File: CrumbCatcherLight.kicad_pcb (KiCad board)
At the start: 2 copper layers, 79.4 x 91.8 mm, 78 parts, among them J1 USB_C_Receptacle_USB2.0, J2 Conn_ARM_SWD_TagConnect_TC203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, Q1 2N7002VC-7, SW10 SW_SPST, SW11 SW_SPST, SW12 SW_SPST, SW13 SW_SPST, SW14 SW_SPST, SW15 SW_SPST, SW16 SW_SPST, SW17 SW_SPST, SW2 SW_SPST, SW3 SW_SPST, SW4 SW_SPST, SW5 SW_SPST, SW6 SW_SPST, SW7 SW_SPST, SW8 SW_SPST, SW9 SW_SPST, U1 ECMF02-2AMX6, U2 XC6206PxxxMR-Regulator_Linear, U3 GD25LQ128DYIGR, U4 RP2040, Y1 12MHz

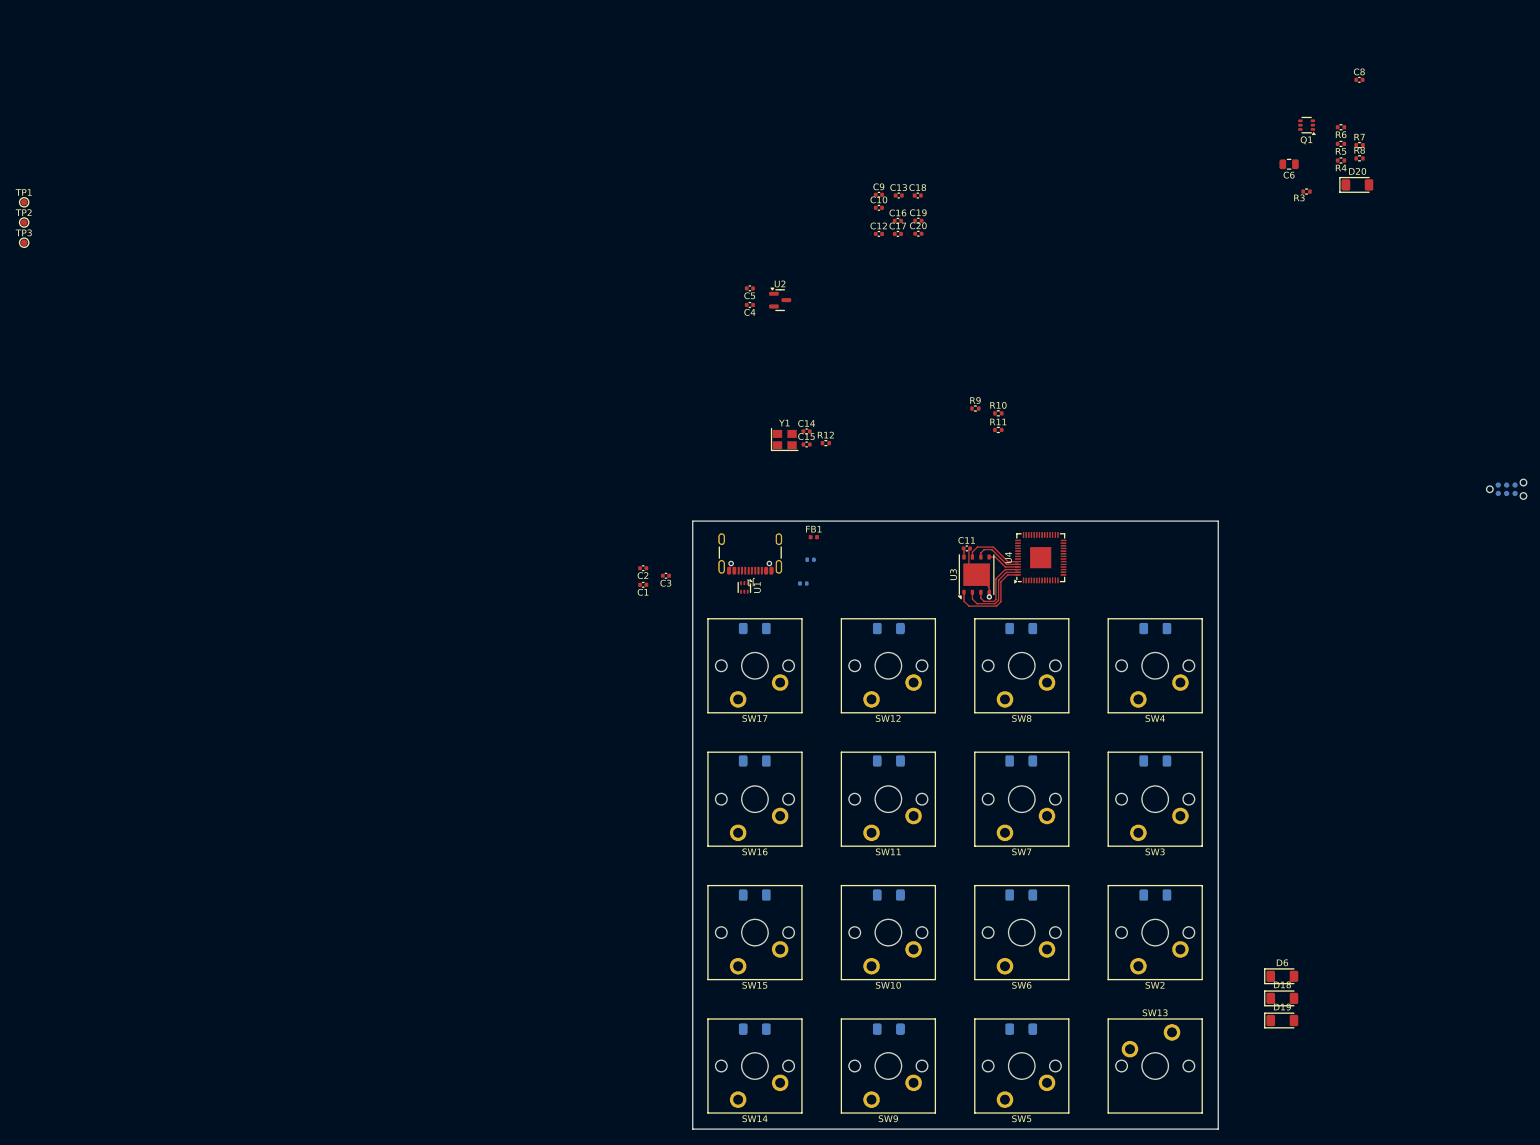
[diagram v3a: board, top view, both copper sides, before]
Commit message: Select last few components, add and cleanup footprints
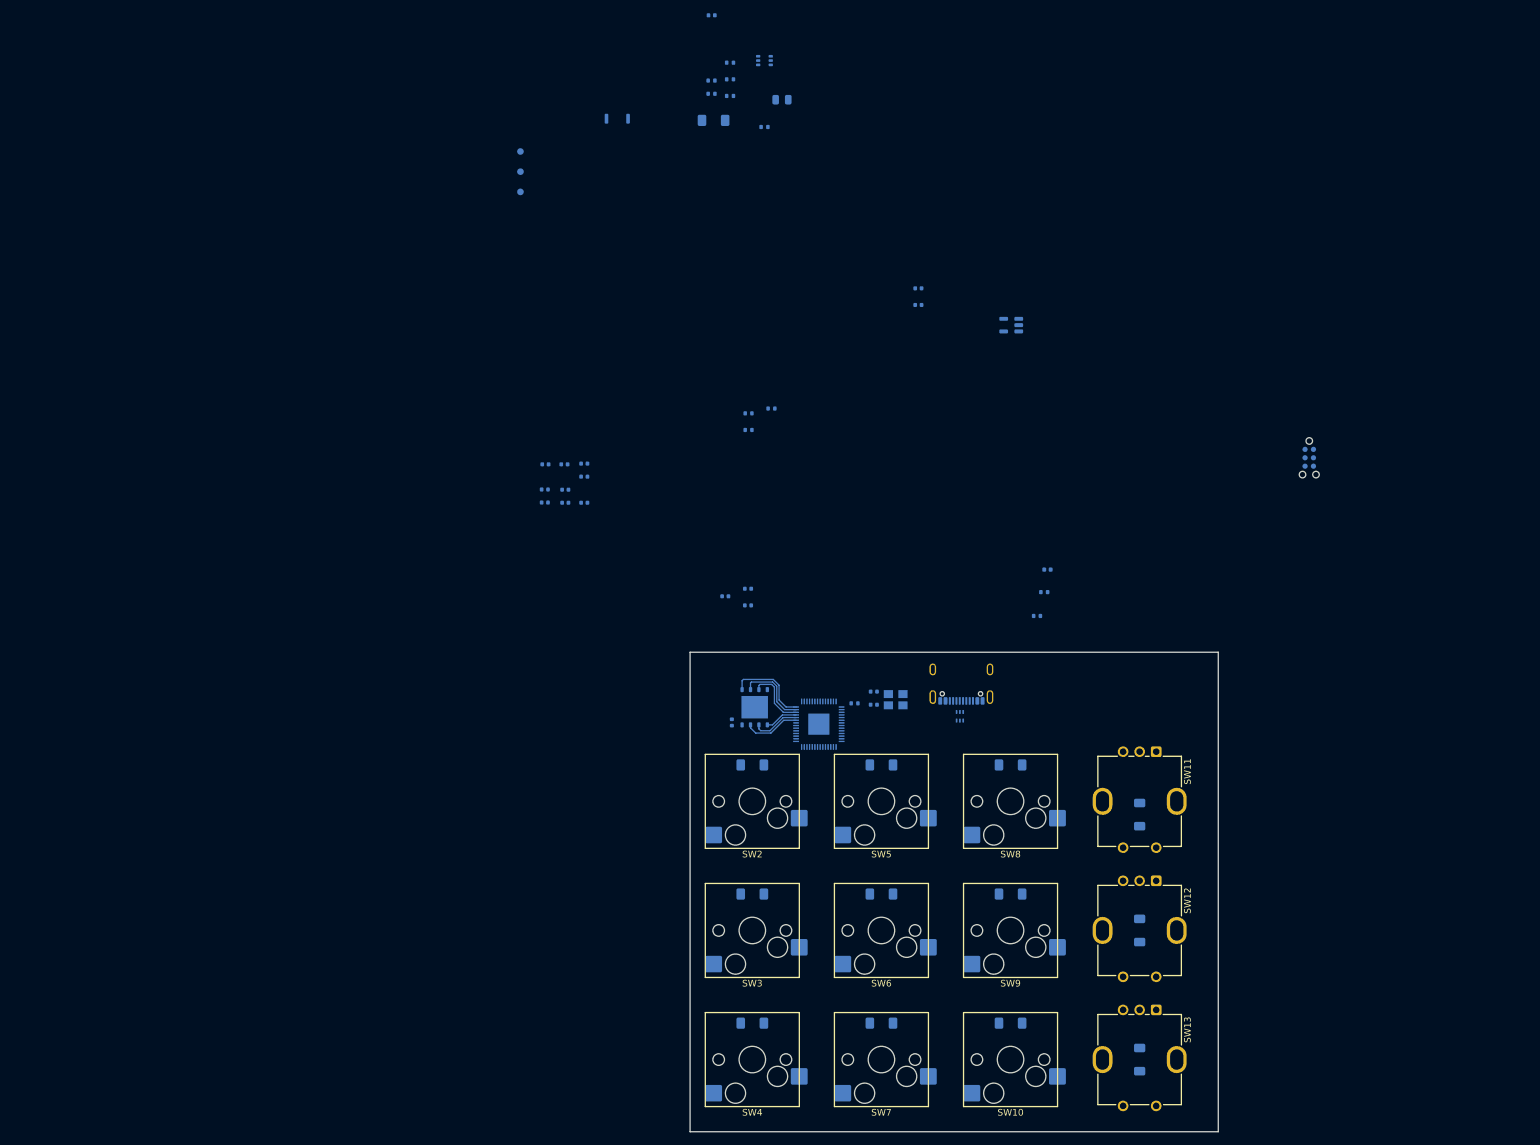
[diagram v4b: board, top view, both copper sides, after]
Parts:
- removed the D13 at (131.6, 105.7)
- removed D14, D15, D16, D17: LL4148, Diode_SMD:D_MiniMELF
- removed the D5 at (151.6, 125.9)
- removed the D9 at (151.6, 85.4)
- removed SW14, SW15, SW16, SW17: SW_SPST, PCM_Switch_Keyboard_Cherry_MX:SW_Cherry_MX_PCB_1.00u
- removed the SW5 at (151.7, 131.5)
- removed the SW8 at (151.7, 71.0)
- removed U2: XC6206PxxxMR-Regulator_Linear, Package_TO_SOT_SMD:SOT-23
- added D12: LL4148, Diode_SMD:D_MiniMELF, B.Cu at (169.5, 111.0)
- added SW1: TL3780AF240QG, Mad_Footprints:SW_TL3780AF240QG, B.Cu at (90.6, -11.6)
- added SW11: PEC11R, Mad_Footprints:RotaryEncoder_Bourns_Vertical_PEC12R-3x17F-Sxxxx, F.Cu at (169.5, 91.5)
- added SW12: PEC11R, Mad_Footprints:RotaryEncoder_Bourns_Vertical_PEC12R-3x17F-Sxxxx, F.Cu at (169.5, 111.0)
- added U5: XC6210B332MR, Package_TO_SOT_SMD:SOT-23-5, B.Cu at (150.1, 19.6)
- C1, C2, C3, C4, C5, C6, D6, FB1, J1, Q1, R10, R11, R12, R3, R4, R5, R6, R7, R8, R9, TP1, TP2, TP3, U1, U3, U4, Y1: moved to B.Cu
- C10: renamed from C11; moved to B.Cu
- C11: renamed from C12; moved to B.Cu
- C12: renamed from C13; moved to B.Cu
- C13: renamed from C14; moved to B.Cu
- C14: renamed from C15; moved to B.Cu
- C15: renamed from C16; moved to B.Cu
- C16: renamed from C17; moved to B.Cu
- C17: renamed from C18; moved to B.Cu
- C18: renamed from C19; moved to B.Cu
- C19: renamed from C20; moved to B.Cu
- C7: renamed from C8; moved to B.Cu
- C8: renamed from C9; moved to B.Cu
- C9: renamed from C10; moved to B.Cu
- D1: renamed from D20; moved to B.Cu
- D11: renamed from D18; moved to B.Cu
- D13: renamed from D19; moved to B.Cu
- SW10: renamed from SW2; footprint PCM_Switch_Keyboard_Cherry_MX:SW_Cherry_MX_PCB_1.00u -> Mad_Footprints:SW_Hotswap_Kailh_MX_1.00u
- SW13: value SW_SPST -> PEC11R; footprint PCM_Switch_Keyboard_Cherry_MX:SW_Cherry_MX_PCB_1.00u -> Mad_Footprints:RotaryEncoder_Bourns_Vertical_PEC12R-3x17F-Sxxxx
- SW2: renamed from SW12; footprint PCM_Switch_Keyboard_Cherry_MX:SW_Cherry_MX_PCB_1.00u -> Mad_Footprints:SW_Hotswap_Kailh_MX_1.00u
- SW3: renamed from SW11; footprint PCM_Switch_Keyboard_Cherry_MX:SW_Cherry_MX_PCB_1.00u -> Mad_Footprints:SW_Hotswap_Kailh_MX_1.00u
- SW4: renamed from SW10; footprint PCM_Switch_Keyboard_Cherry_MX:SW_Cherry_MX_PCB_1.00u -> Mad_Footprints:SW_Hotswap_Kailh_MX_1.00u
- SW5: renamed from SW9; footprint PCM_Switch_Keyboard_Cherry_MX:SW_Cherry_MX_PCB_1.00u -> Mad_Footprints:SW_Hotswap_Kailh_MX_1.00u
- SW6: renamed from SW7; footprint PCM_Switch_Keyboard_Cherry_MX:SW_Cherry_MX_PCB_1.00u -> Mad_Footprints:SW_Hotswap_Kailh_MX_1.00u
- SW7: renamed from SW6; footprint PCM_Switch_Keyboard_Cherry_MX:SW_Cherry_MX_PCB_1.00u -> Mad_Footprints:SW_Hotswap_Kailh_MX_1.00u
- SW8: renamed from SW4; footprint PCM_Switch_Keyboard_Cherry_MX:SW_Cherry_MX_PCB_1.00u -> Mad_Footprints:SW_Hotswap_Kailh_MX_1.00u
- SW9: renamed from SW3; footprint PCM_Switch_Keyboard_Cherry_MX:SW_Cherry_MX_PCB_1.00u -> Mad_Footprints:SW_Hotswap_Kailh_MX_1.00u
- moved R7 98.4 mm to (104.8, -17.4), turned to 180 degrees
- moved R8 98.4 mm to (104.8, -15.4), turned to 180 degrees
- moved C7 98.3 mm to (104.9, -27.2), turned to 180 degrees
- moved D1 97.7 mm to (105.2, -11.3), turned to 180 degrees
- moved R4 92.8 mm to (107.6, -15.0), turned to 0 degrees
- moved R5 92.8 mm to (107.6, -17.6), turned to 0 degrees
- moved R6 92.8 mm to (107.6, -20.1), turned to 0 degrees
- moved Q1 82.5 mm to (112.8, -20.4), turned to 0 degrees
- moved R3 82.4 mm to (112.8, -10.3), turned to 0 degrees
- moved C6 77.2 mm to (115.5, -14.5), turned to 0 degrees
- moved TP1 75.3 mm to (76.0, -6.65), turned to 180 degrees
- moved TP2 75.3 mm to (76.0, -3.60), turned to 180 degrees
- moved TP3 75.3 mm to (76.0, -0.55), turned to 180 degrees
- moved C18 69.5 mm to (79.7, 44.4), turned to 180 degrees
- moved C19 69.5 mm to (79.7, 46.4), turned to 180 degrees
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- renumbered D2 to D10, D12 to D2, D11 to D3, D10 to D4, D7 to D5, D8 to D7, D4 to D8, D3 to D9
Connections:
- D10 pad 1: Row1 -> Row2
- D11 pad 1: Row1 -> Row0
- D13 pad 1: Row3 -> Row2
- D13 pad 2: Net-(D19-A) -> Net-(D13-A)
- D2 pad 1: Row3 -> Row0
- D3 pad 1: Row2 -> Row1
- D4 pad 1: Row1 -> Row2
- D5 pad 1: Row2 -> Row0
- D7 pad 1: Row3 -> Row2
- D8 pad 1: Row3 -> Row0
- D9 pad 1: Row2 -> Row1
- SW10 pad 2: Col0 -> Col2
- SW2 pad 2: Col2 -> Col0
- SW3 pad 2: Col2 -> Col0
- SW4 pad 2: Col2 -> Col0
- SW8 pad 2: Col0 -> Col2
- SW9 pad 2: Col0 -> Col2
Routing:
- net GND: track 10.4 -> 3.33 mm, vias 1 -> 0
- net IOVDD: track 1.32 -> 0.00 mm
- net /RP2040/QSPI_SD2: track 10.5 -> 9.48 mm
- net /RP2040/QSPI_nCS: track 13.5 -> 12.6 mm
- net /RP2040/QSPI_SD1: track 11.9 -> 11.0 mm
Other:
- board size 79.4 x 91.8 mm -> 79.8 x 72.4 mm

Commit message: Update lib, finish off rotary encoder schematic, reselect diode for reset circuit
Update RP2040, rename bom only footprint, add mechanical footprint. Add PCB symbol
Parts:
- removed D1: LL4148, Diode_SMD:D_MiniMELF
- added D14: RB520S30, Diode_SMD:D_SOD-523, B.Cu at (111.3, -15.6)
- added R13: 2K2, Resistor_SMD:R_0402_1005Metric, B.Cu at (121.1, 53.7)
- added R14: 5K1, Resistor_SMD:R_0402_1005Metric, B.Cu at (121.1, 55.6)
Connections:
- net /RP2040/GPIO0 renamed /RP2040/0_TX0
- net /RP2040/GPIO1 renamed /RP2040/1_RX0
- net /RP2040/GPIO2 renamed /RP2040/2_SDA1
- net /RP2040/GPIO26 renamed /RP2040/A0
- net /RP2040/GPIO27 renamed /RP2040/A1
- net /RP2040/GPIO28 renamed /RP2040/A2
- net /RP2040/GPIO29 renamed /RP2040/A3
- net /RP2040/GPIO3 renamed /RP2040/3_SCL1
- net /RP2040/GPIO4 renamed /RP2040/4
- net /RP2040/GPIO5 renamed /RP2040/5
- net /RP2040/GPIO6 renamed /RP2040/6
- net /RP2040/GPIO7 renamed /RP2040/7
- net /RP2040/GPIO8 renamed /RP2040/8
- net /RP2040/GPIO9 renamed /RP2040/9
- net Col0 renamed /Switches/Col0
- net Col1 renamed /Switches/Col1
- net Col2 renamed /Switches/Col2
- net Col3 renamed /Switches/Col3
- net Row0 renamed /Switches/Row0
- net Row1 renamed /Switches/Row1
- net Row2 renamed /Switches/Row2
- SW11 pad A: unconnected-(SW11-PadA) -> /Switches/ENC1A
- SW11 pad B: unconnected-(SW11-PadB) -> /Switches/ENC1B
- SW11 pad C: unconnected-(SW11-PadC) -> /Switches/GND
- SW12 pad A: unconnected-(SW12-PadA) -> /Switches/ENC2A
- SW12 pad B: unconnected-(SW12-PadB) -> /Switches/ENC2B
- SW12 pad C: unconnected-(SW12-PadC) -> /Switches/GND
- SW13 pad A: unconnected-(SW13-PadA) -> /Switches/ENC3A
- SW13 pad B: unconnected-(SW13-PadB) -> /Switches/ENC3B
- SW13 pad C: unconnected-(SW13-PadC) -> /Switches/GND
- U4 pad 13: /RP2040/GPIO10 -> unconnected-(U4-GPIO10-Pad13)
- U4 pad 14: /RP2040/GPIO11 -> unconnected-(U4-GPIO11-Pad14)
- U4 pad 15: /RP2040/GPIO12 -> unconnected-(U4-GPIO12-Pad15)
- U4 pad 16: /RP2040/GPIO13 -> unconnected-(U4-GPIO13-Pad16)
- U4 pad 17: /RP2040/GPIO14 -> unconnected-(U4-GPIO14-Pad17)
- U4 pad 18: /RP2040/GPIO15 -> unconnected-(U4-GPIO15-Pad18)
- U4 pad 27: /RP2040/GPIO16 -> unconnected-(U4-GPIO16-Pad27)
- U4 pad 28: /RP2040/GPIO17 -> unconnected-(U4-GPIO17-Pad28)
- U4 pad 29: /RP2040/GPIO18 -> unconnected-(U4-GPIO18-Pad29)

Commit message: Finish off rotary encoders, add EMC zone for USB, fix few remaining lib links, fix DRC
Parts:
- removed the R9 at (113.9, 32.2)
- added C20: 100nF, Capacitor_SMD:C_0402_1005Metric, B.Cu at (83.3, 21.6)
- added C21: 100nF, Capacitor_SMD:C_0402_1005Metric, B.Cu at (83.3, 23.5)
- added C22: 100nF, Capacitor_SMD:C_0402_1005Metric, B.Cu at (83.3, 25.5)
- added C23: 100nF, Capacitor_SMD:C_0402_1005Metric, B.Cu at (83.3, 27.5)
- added C24: 100nF, Capacitor_SMD:C_0402_1005Metric, B.Cu at (83.3, 29.4)
- added C25: 100nF, Capacitor_SMD:C_0402_1005Metric, B.Cu at (83.3, 31.4)
- added FB2: BLM15PX330SN1D, Inductor_SMD:L_0402_1005Metric, B.Cu at (135.6, 36.6)
- added U2: PCB, Mad_Footprints:BOM, B.Cu at (134.9, 33.3)
- J1: value USB_C_Receptacle_USB2.0 -> USB_C_Receptacle
- renumbered C15 to C13, C13 to C14, C14 to C15, C6 to C5, C5 to C6, D14 to D1, R11 to R10, R12 to R11, R13 to R12, R14 to R13, R4 to R3, R3 to R4, R10 to R9, U5 to U3, U3 to U4, U4 to U5
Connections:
- net /RP2040/0_TX0 renamed /LED_TX0
- net /RP2040/1_RX0 renamed /DATA_RX0
- net /RP2040/2_SDA1 renamed /2_SDA1
- net /RP2040/3_SCL1 renamed /3_SCL1
- net /RP2040/A0 renamed /RP2040/GPIO26
- net /RP2040/A1 renamed /RP2040/GPIO27
- net /RP2040/A2 renamed /RP2040/GPIO28
- net /RP2040/A3 renamed /RP2040/GPIO29
- net DVDD renamed /RP2040/1V1
- net IOVDD renamed /RP2040/3V3
- D10 pad 1: /Switches/Row2 -> /RP2040/GPIO6
- D11 pad 1: /Switches/Row0 -> /RP2040/GPIO4
- D12 pad 1: /Switches/Row1 -> /RP2040/GPIO5
- D13 pad 1: /Switches/Row2 -> /RP2040/GPIO6
- D2 pad 1: /Switches/Row0 -> /RP2040/GPIO4
- D3 pad 1: /Switches/Row1 -> /RP2040/GPIO5
- D4 pad 1: /Switches/Row2 -> /RP2040/GPIO6
- D5 pad 1: /Switches/Row0 -> /RP2040/GPIO4
- D6 pad 1: /Switches/Row1 -> /RP2040/GPIO5
- D7 pad 1: /Switches/Row2 -> /RP2040/GPIO6
- D8 pad 1: /Switches/Row0 -> /RP2040/GPIO4
- D9 pad 1: /Switches/Row1 -> /RP2040/GPIO5
- J1 pad A1: GND -> /PreFIlterGND
- J1 pad A12: GND -> /PreFIlterGND
- J1 pad B1: GND -> /PreFIlterGND
- J1 pad B12: GND -> /PreFIlterGND
- J1 pad S1: GND -> /PreFIlterGND
- R1 pad 2: GND -> /PreFIlterGND
- R10 pad 1: /RP2040/D_N -> /RP2040/USB_D-
- R2 pad 2: GND -> /PreFIlterGND
- R9 pad 1: /RP2040/D_P -> /RP2040/USB_D+
- SW10 pad 2: /Switches/Col2 -> /RP2040/GPIO9
- SW11 pad A: /Switches/ENC1A -> /RP2040/GPIO11
- SW11 pad B: /Switches/ENC1B -> /RP2040/GPIO12
- SW11 pad C: /Switches/GND -> GND
- SW11 pad S1: /Switches/Col3 -> /RP2040/GPIO10
- SW12 pad A: /Switches/ENC2A -> /RP2040/GPIO13
- SW12 pad B: /Switches/ENC2B -> /RP2040/GPIO14
- SW12 pad C: /Switches/GND -> GND
- SW12 pad S1: /Switches/Col3 -> /RP2040/GPIO10
- SW13 pad A: /Switches/ENC3A -> /RP2040/GPIO15
- SW13 pad B: /Switches/ENC3B -> /RP2040/GPIO16
- SW13 pad C: /Switches/GND -> GND
- SW13 pad S1: /Switches/Col3 -> /RP2040/GPIO10
- SW2 pad 2: /Switches/Col0 -> /RP2040/GPIO7
- SW3 pad 2: /Switches/Col0 -> /RP2040/GPIO7
- SW4 pad 2: /Switches/Col0 -> /RP2040/GPIO7
- SW5 pad 2: /Switches/Col1 -> /RP2040/GPIO8
- SW6 pad 2: /Switches/Col1 -> /RP2040/GPIO8
- SW7 pad 2: /Switches/Col1 -> /RP2040/GPIO8
- SW8 pad 2: /Switches/Col2 -> /RP2040/GPIO9
- SW9 pad 2: /Switches/Col2 -> /RP2040/GPIO9
- U1 pad 3: GND -> /PreFIlterGND
- U1 pad 5: /USB_D+ -> /RP2040/USB_D+
- U1 pad 6: /USB_D- -> /RP2040/USB_D-
- U5 pad 11: /RP2040/8 -> /RP2040/GPIO8
- U5 pad 12: /RP2040/9 -> /RP2040/GPIO9
- U5 pad 13: unconnected-(U4-GPIO10-Pad13) -> /RP2040/GPIO10
- U5 pad 14: unconnected-(U4-GPIO11-Pad14) -> /RP2040/GPIO11
- U5 pad 15: unconnected-(U4-GPIO12-Pad15) -> /RP2040/GPIO12
- U5 pad 16: unconnected-(U4-GPIO13-Pad16) -> /RP2040/GPIO13
- U5 pad 17: unconnected-(U4-GPIO14-Pad17) -> /RP2040/GPIO14
- U5 pad 18: unconnected-(U4-GPIO15-Pad18) -> /RP2040/GPIO15
- U5 pad 27: unconnected-(U4-GPIO16-Pad27) -> /RP2040/GPIO16
- U5 pad 28: unconnected-(U4-GPIO17-Pad28) -> /RP2040/GPIO17
- U5 pad 29: unconnected-(U4-GPIO18-Pad29) -> /RP2040/GPIO18
- U5 pad 30: /RP2040/GPIO19 -> /RP2040/VBUS_DETECT
- U5 pad 6: /RP2040/4 -> /RP2040/GPIO4
- U5 pad 7: /RP2040/5 -> /RP2040/GPIO5
- U5 pad 8: /RP2040/6 -> /RP2040/GPIO6
- U5 pad 9: /RP2040/7 -> /RP2040/GPIO7
